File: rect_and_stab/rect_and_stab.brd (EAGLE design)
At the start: 44 x 44 mm, 42 parts, among them Q1 BSZ0902NSI, Q2 BSZ0902NSI, Q3 BSZ0902NSI, Q4 BSZ0902NSI, Q5 BSZ0902NSI, Q6 BSZ0902NSI, Q7 BSZ0902NSI, Q8 BSZ0902NSI

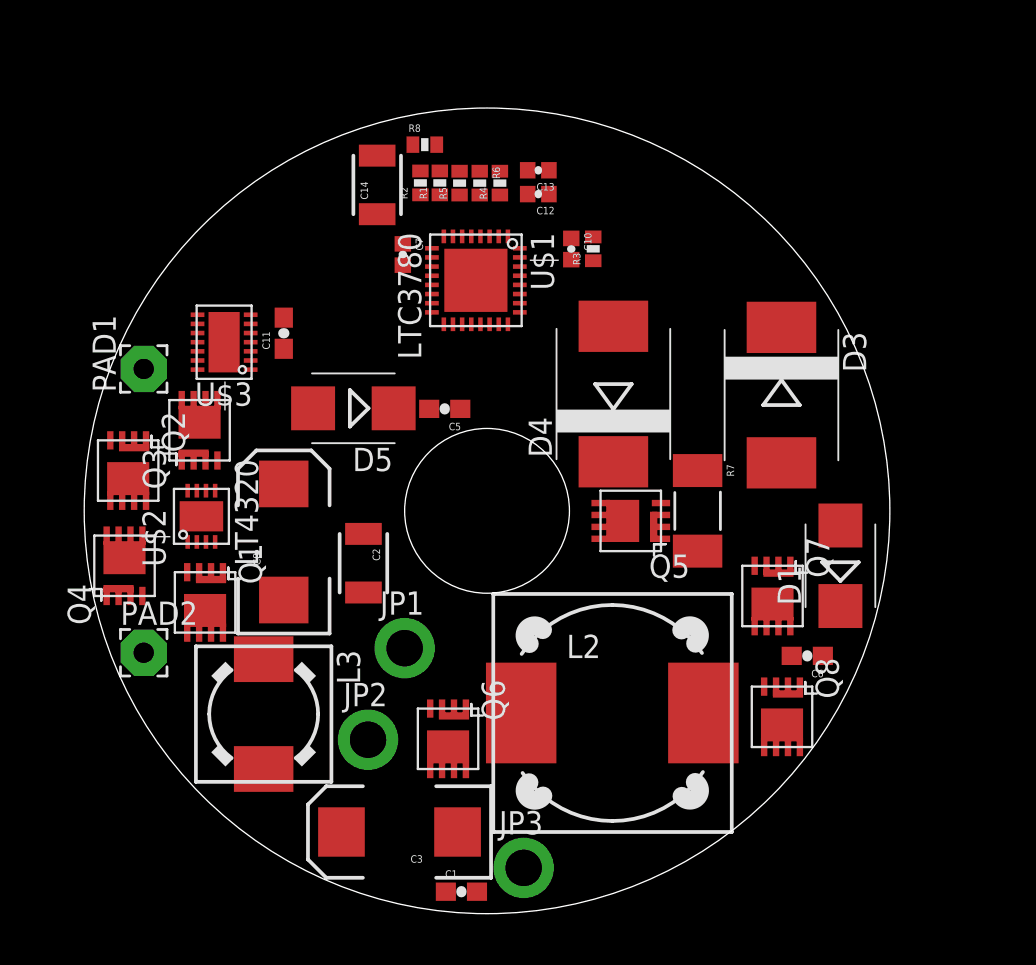
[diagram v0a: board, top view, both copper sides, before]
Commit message: board routed and secondary protection removed
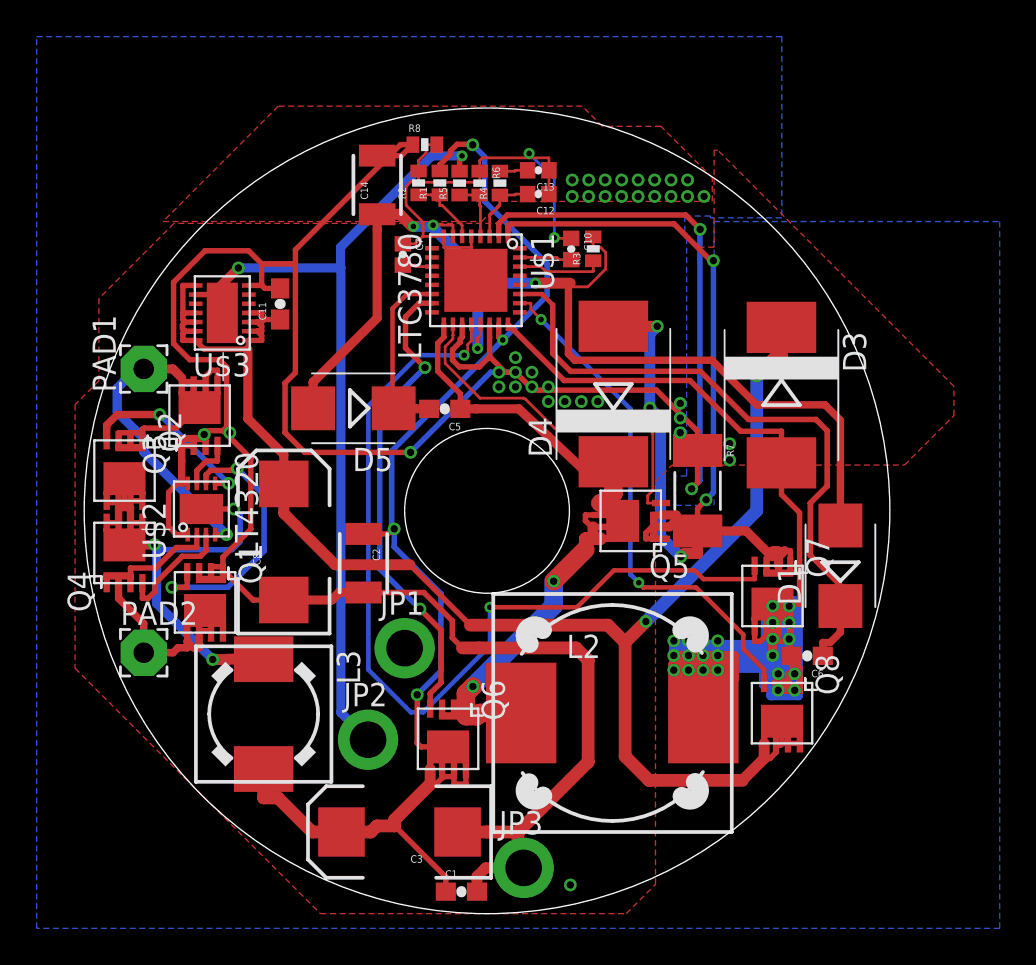
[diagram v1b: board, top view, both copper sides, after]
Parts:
- moved C11 1.61 mm to (10.7, 33.3)
- moved U$3 1.60 mm to (7.54, 32.8)
- moved R7 1.10 mm to (33.5, 23.1)
- moved Q3 0.80 mm to (6.30, 27.2)
- moved Q4 0.70 mm to (2.20, 19.7)
- moved U$2 0.40 mm to (6.40, 22.1)
- moved Q2 0.20 mm to (2.20, 24.2)
- moved Q8 0.20 mm to (38.1, 10.9)
- moved R2 0.10 mm to (18.3, 39.9)
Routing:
- net GND: track 0.00 -> 170.4 mm, vias 0 -> 44
- net N$11: track 0.00 -> 115.8 mm, vias 0 -> 23
- net N$22: track 0.00 -> 87.4 mm, vias 0 -> 2
- net +12V: track 0.00 -> 70.8 mm, vias 0 -> 4
- net N$26: track 0.00 -> 62.0 mm, vias 0 -> 4
- net N$23: track 0.00 -> 60.4 mm, vias 0 -> 5
- net N$10: track 0.00 -> 50.1 mm, vias 0 -> 2
- net N$13: track 0.00 -> 46.9 mm, vias 0 -> 2
- net N$16: track 0.00 -> 42.2 mm, vias 0 -> 2
- net N$5: track 0.00 -> 35.4 mm
- net AGND: track 0.00 -> 30.4 mm, vias 0 -> 2
- net N$9: track 0.00 -> 29.6 mm, vias 0 -> 3
- net N$14: track 0.00 -> 28.3 mm, vias 0 -> 2
- net N$2: track 0.00 -> 27.4 mm, vias 0 -> 1
- net N$17: track 0.00 -> 26.2 mm, vias 0 -> 2
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- added copper zone on layer 1, net GND
- added copper zone on layer 16, net GND

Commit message: mirrored charger board. this version has been ordered (charger&rect_and_stab)
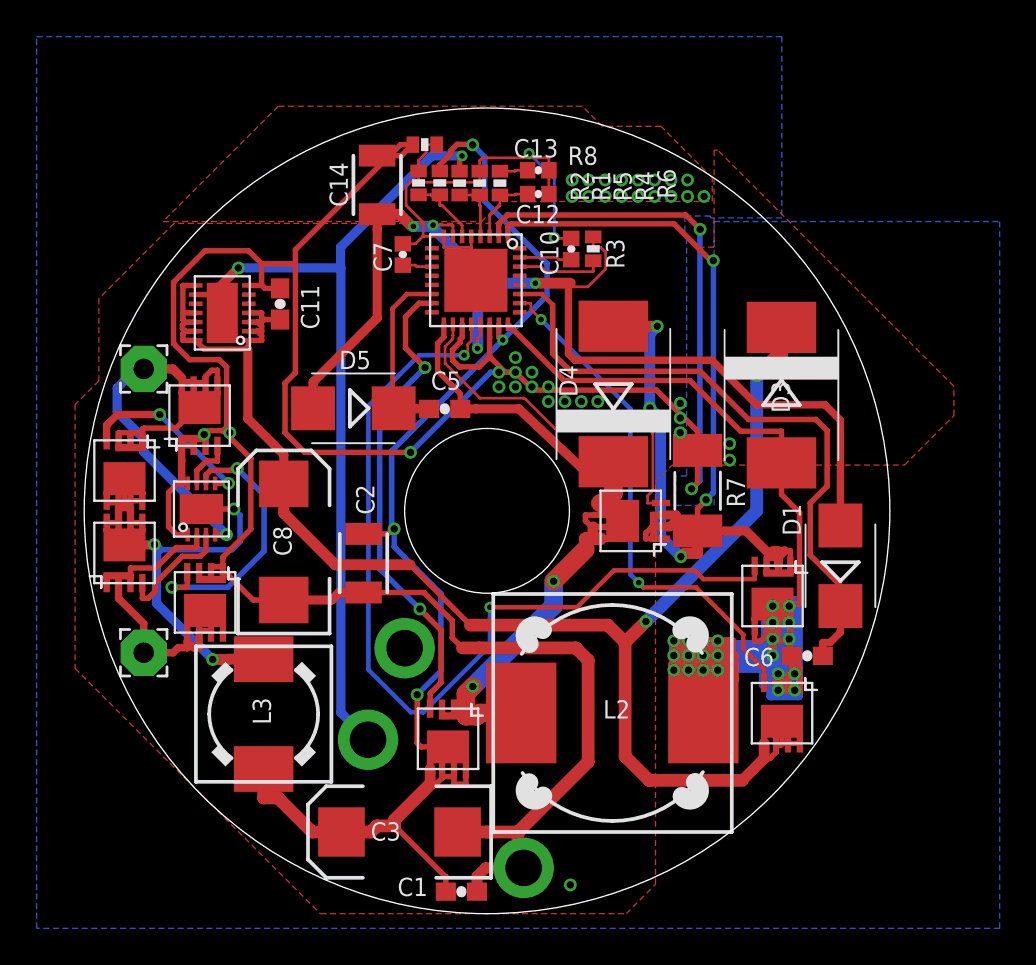
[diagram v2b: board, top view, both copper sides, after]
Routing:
- net N$11: track 115.8 -> 144.2 mm
